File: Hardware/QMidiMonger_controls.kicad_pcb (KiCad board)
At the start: 2 copper layers, 40 x 100 mm, 23 parts, among them J1 CV_Out, J2 CV_Out, J20 Conn_01x09_Female, J21 Conn_01x08_Female, J22 Conn_01x08_Female, J23 Conn_01x08_Female, J3 CV_Out, J4 Gate_Out, J5 Gate_Out, J6 Gate_Out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

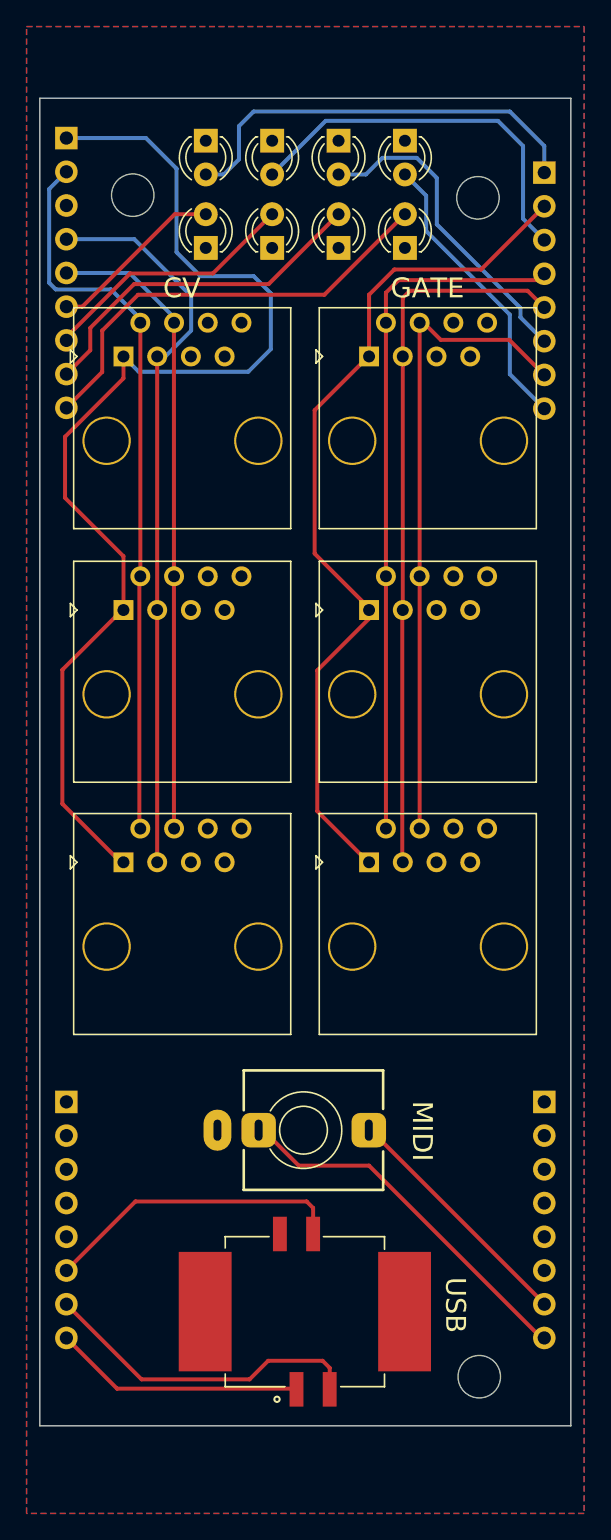
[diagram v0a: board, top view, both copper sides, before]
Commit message: Added panel PCB; added board interconnects
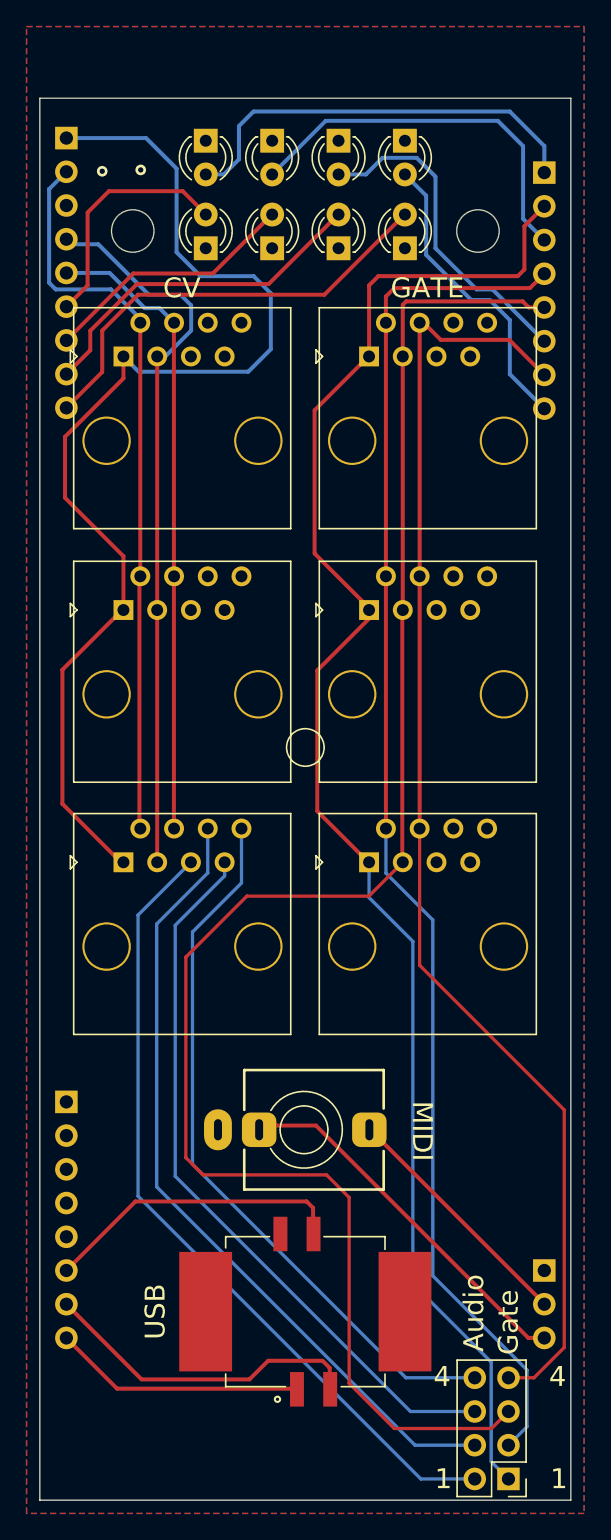
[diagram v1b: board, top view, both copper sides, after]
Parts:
- removed H3: MountingHole, MountingHole:MountingHole_3.2mm_M3_ISO14580
- added D9: 3d_Model_Dummy, Custom_Footprints:3D_Dummy, F.Cu at (116.0, 93.3)
- added J9: Conn_02x04_Odd_Even, Connector_PinHeader_2.54mm:PinHeader_2x04_P2.54mm_Vertical, F.Cu at (131.3, 148.4)
- J23: value Conn_01x08_Female -> Conn_01x03_Female; footprint Socket_Strips:Socket_Strip_Straight_1x08_Pitch2.54mm -> Connector_PinHeader_2.54mm:PinHeader_1x03_P2.54mm_Vertical
- moved J23 12.7 mm to (134.0, 132.7)
- moved H1 2.70 mm to (103.0, 54.4)
- moved H2 2.50 mm to (129.0, 54.4)
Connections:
- J23 pad 1: /GATE7_LED_OUT -> GND
- J23 pad 2: /GATE6_LED_OUT -> /MIDI_DATA
- J23 pad 3: /GATE8_LED_OUT -> /MIDI_VREF
- J3 pad 5: unconnected-(J3-Pad5) -> /AUDIO_IN1
- J3 pad 6: unconnected-(J3-Pad6) -> /AUDIO_IN2
- J3 pad 7: unconnected-(J3-Pad7) -> /AUDIO_IN3
- J3 pad 8: unconnected-(J3-Pad8) -> /AUDIO_IN4
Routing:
- net /GATE3_OUT: track 53.6 -> 128.5 mm
- net /AUDIO_IN1: track 0.00 -> 61.0 mm
- net /AUDIO_IN2: track 0.00 -> 60.6 mm
- net /AUDIO_IN3: track 0.00 -> 55.1 mm
- net /AUDIO_IN4: track 0.00 -> 54.7 mm
- net /GATE1_OUT: track 65.0 -> 118.1 mm
- net /GATE2_OUT: track 52.6 -> 103.9 mm
- net /GATE4_OUT: track 49.2 -> 98.0 mm
- net /CV1_LED_OUT: track 13.4 -> 18.0 mm
- net /GATE4_LED_OUT: track 22.0 -> 22.8 mm
- net /GATE3_LED_OUT: track 24.2 -> 24.9 mm
- net GND: track 0.08 -> 0.00 mm, vias 0 -> 2
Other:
- board size 40 x 100 mm -> 40 x 105.6 mm
- board text added: "1"
- board text added: "4"
- board text added: "Audio"
- board text added: "Gate"

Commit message: Added inter-board connector
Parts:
- added H3: MountingHole, MountingHole:MountingHole_3.2mm_M3_ISO14580, F.Cu at (101.4, 145.3)
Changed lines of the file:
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@@
+  )
+  (footprint "MountingHole:MountingHole_3.2mm_M3_ISO14580" (layer "F.Cu")
+    (at 101.4 145.3)
+    (descr "Mounting Hole 3.2mm, no annular, M3, ISO14580")
+    (tags "mounting hole 3.2mm no annular m3 iso14580")
+    (property "Sheetfile" "QMidiMonger_controls.kicad_sch")
+    (property "Sheetname" "")
+    (attr exclude_from_pos_files)
+    (fp_text reference "H3" (at 0 -3.75) (layer "F.SilkS")
+      (effects (font (size 1 1) (thickness 0.15)))
+    )
+    (fp_text value "MountingHole" (at 0 3.75) (layer "F.Fab")
+      (effects (font (size 1 1) (thickness 0.15)))
+    )
+    (fp_text user "${REFERENCE}" (at 0 0) (layer "F.Fab")
+      (effects (font (size 1 1) (thickness 0.15)))
+    )
+    (fp_circle (center 0 0) (end 2.75 0) (layer "Cmts.User") (width 0.15) (fill none))
+    (fp_circle (center 0 0) (end 3 0) (layer "F.CrtYd") (width 0.05) (fill none))
+    (pad "" np_thru_hole circle (at 0 0) (size 3.2 3.2) (drill 3.2) (layers *.Cu *.Mask))
   )
   (footprint "MountingHole:MountingHole_3.2mm_M3_ISO14580" (layer "F.Cu")

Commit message: Cleaned up Panel and Controls
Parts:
- added H4: MountingHole, MountingHole:MountingHole_3.2mm_M3_ISO14580, F.Cu at (130.7, 142.4)
- D1, D2, D3, D4, D5, D6, D7, D8: footprint LEDs:LED_D3.0mm -> Custom_Footprints:LED_D3.0mm
- moved J9 22.9 mm to (130.9, 125.5)
- moved H3 2.90 mm to (101.3, 142.4)
- moved D5 1.70 mm to (108.5, 54.0)
- moved D6 1.70 mm to (113.5, 54.0)
- moved D7 1.70 mm to (118.5, 54.0)
- moved D8 1.70 mm to (123.5, 54.0)
- turned J8 to 0 degrees
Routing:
- net /GATE3_OUT: track 128.5 -> 74.2 mm
- net /GATE4_OUT: track 98.0 -> 70.3 mm
- net /AUDIO_IN4: track 54.7 -> 27.5 mm
- net /AUDIO_IN2: track 60.6 -> 34.6 mm
- net /AUDIO_IN3: track 55.1 -> 29.5 mm
- net /AUDIO_IN1: track 61.0 -> 37.1 mm
- net /GATE1_OUT: track 118.1 -> 95.0 mm
- net /GATE2_OUT: track 103.9 -> 80.8 mm
- net /USB_DM: track 24.6 -> 18.3 mm
- net /GATE1_LED_OUT: track 32.0 -> 26.4 mm
- net /USB_DP: track 22.3 -> 26.5 mm
- net /USB_VBUS: track 18.9 -> 22.5 mm
- net /GATE4_LED_OUT: track 22.8 -> 24.1 mm
- net /GATE3_LED_OUT: track 24.9 -> 26.1 mm
- net /GATE2_LED_OUT: track 29.1 -> 29.8 mm
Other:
- board size 40 x 105.6 mm -> 40 x 102.5 mm
- board text added: "Mountjoy Modular 2023 Quad MIDI Monger Controls v1.0"
- board text removed: "Mountjoy Modular Quad MIDI Monger Controls v1.0"
